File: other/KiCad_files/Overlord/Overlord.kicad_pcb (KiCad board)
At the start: 2 copper layers, 155.1 x 86.1 mm, 121 parts, among them J1 RJ45x2, J2 Screw_Terminal_01x09, J3 Screw_Terminal_01x09, J4 Screw_Terminal_01x09, J5 Screw_Terminal_01x09, J6 Screw_Terminal_01x09, J7 Conn_01x06_Male, Q1 2N7002E, Q2 2N7002E, Q3 2N7002E, Q4 2N7002E, Q5 2N7002E, Q6 2N7002E, U1 74HC4052D,653, U2 74HC4052D,653, U3 74HC4052D,653, U4 74HC4052D,653, U5 LM2575D2T-5G, U6 SN65HVD230, U7 MAX485ESA+T, U8 AP63203WU-7, U9 MAX485ESA+T

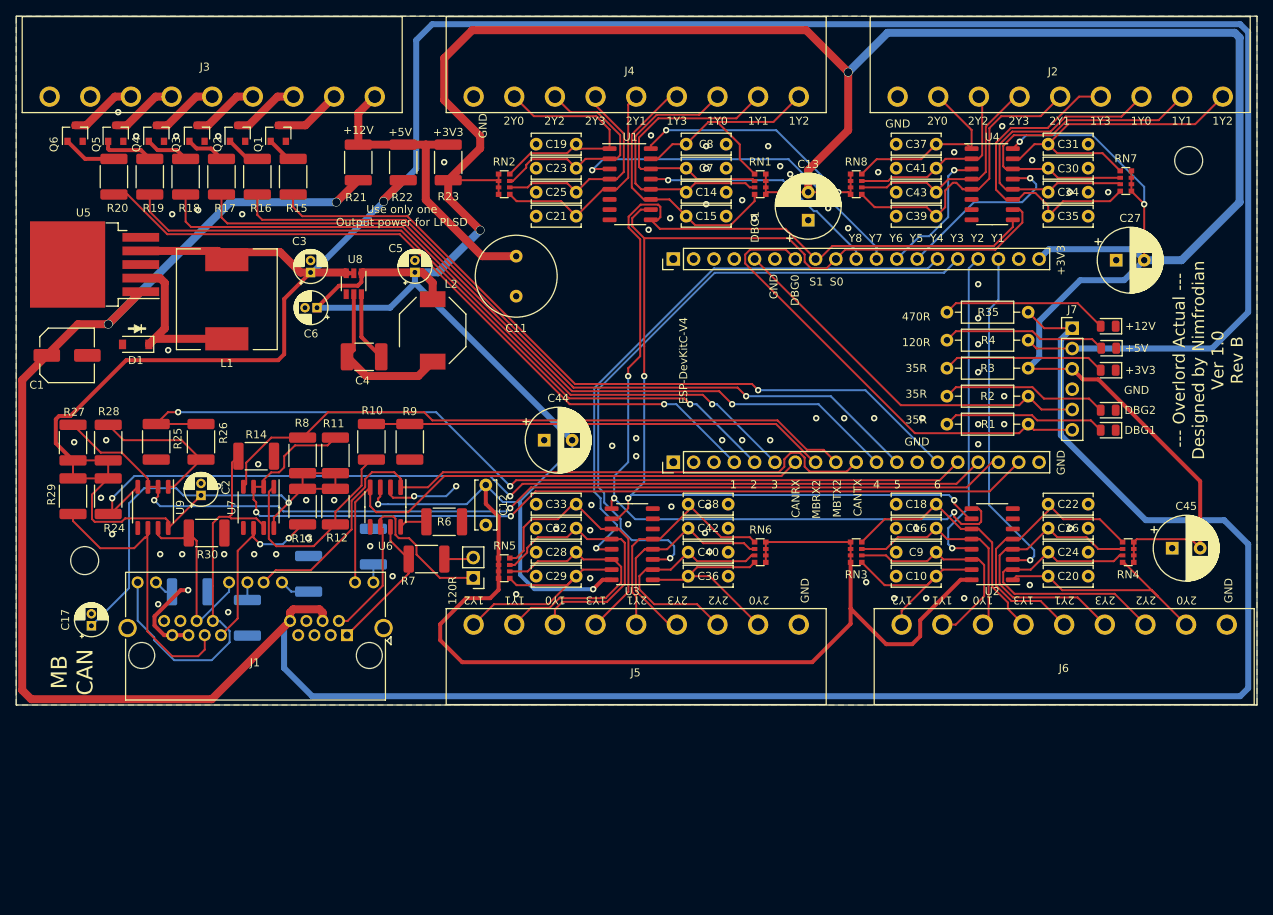
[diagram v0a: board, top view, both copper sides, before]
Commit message: Added LED pins for quick status display,  updated schematic (still need to update PCB),
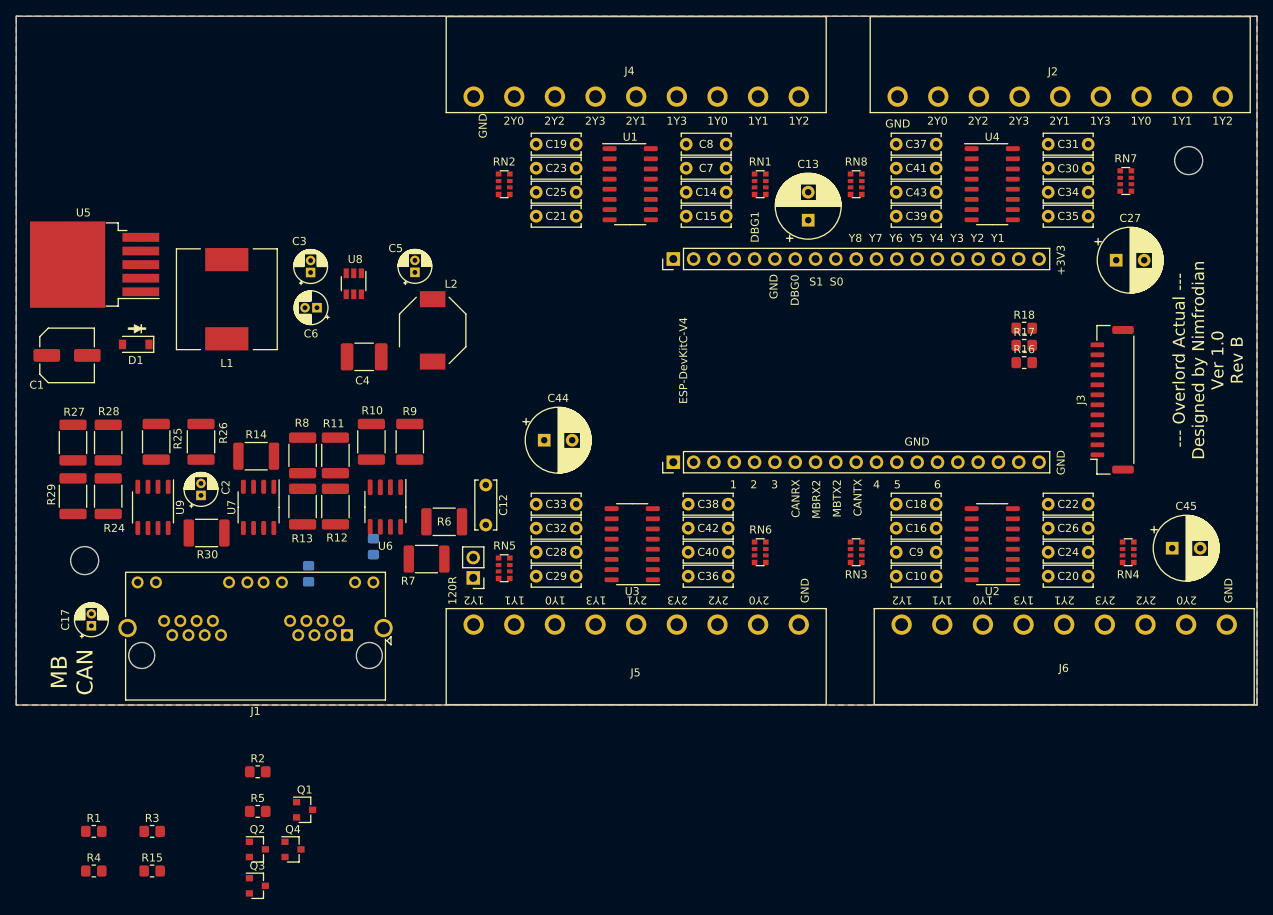
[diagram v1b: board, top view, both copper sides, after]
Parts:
- removed C11: 1800uF, Capacitor_THT:C_Radial_D10.0mm_H20.0mm_P5.00mm
- removed D2, D3, D4, D5, D6: LED, LED_SMD:LED_0805_2012Metric
- removed J7: Conn_01x06_Male, Connector_PinHeader_2.54mm:PinHeader_1x06_P2.54mm_Vertical
- removed Q5, Q6: 2N7002E, Package_TO_SOT_SMD:SOT-23
- removed R19, R20: 1K, Resistor_SMD:R_1812_4532Metric_Pad1.30x3.40mm_HandSolder
- removed R21: V_select_12V, Resistor_SMD:R_1812_4532Metric_Pad1.30x3.40mm_HandSolder
- removed R22: V_select_5V, Resistor_SMD:R_1812_4532Metric_Pad1.30x3.40mm_HandSolder
- removed R23: V_select_3V3, Resistor_SMD:R_1812_4532Metric_Pad1.30x3.40mm_HandSolder
- removed R32, R34: 220, Resistor_SMD:R_1812_4532Metric_Pad1.30x3.40mm_HandSolder
- removed R35: 470R, Resistor_THT:R_Axial_DIN0207_L6.3mm_D2.5mm_P10.16mm_Horizontal
- added R5: 10K, Resistor_SMD:R_0805_2012Metric_Pad1.20x1.40mm_HandSolder, F.Cu at (55.6, 124.8)
- J3: value Screw_Terminal_01x09 -> Conn_01x12_Female; footprint TerminalBlockCustom:TerminalBlock_9_5.08mm -> Connector_Molex:Molex_CLIK-Mate_502386-1270_1x12-1MP_P1.25mm_Horizontal
- R1, R2: value 35R -> 5K; footprint Resistor_THT:R_Axial_DIN0207_L6.3mm_D2.5mm_P10.16mm_Horizontal -> Resistor_SMD:R_0805_2012Metric_Pad1.20x1.40mm_HandSolder
- R15: value 1K -> 10K; footprint Resistor_SMD:R_1812_4532Metric_Pad1.30x3.40mm_HandSolder -> Resistor_SMD:R_0805_2012Metric_Pad1.20x1.40mm_HandSolder
- R16, R17, R18: value 1K -> 220; footprint Resistor_SMD:R_1812_4532Metric_Pad1.30x3.40mm_HandSolder -> Resistor_SMD:R_0805_2012Metric_Pad1.20x1.40mm_HandSolder
- R3: value 35R -> 10K; footprint Resistor_THT:R_Axial_DIN0207_L6.3mm_D2.5mm_P10.16mm_Horizontal -> Resistor_SMD:R_0805_2012Metric_Pad1.20x1.40mm_HandSolder
- R31, R33: value 220 -> 5K; footprint Resistor_SMD:R_1812_4532Metric_Pad1.30x3.40mm_HandSolder -> Resistor_SMD:R_0805_2012Metric_Pad1.20x1.40mm_HandSolder
- R4: value 120R -> 10K; footprint Resistor_THT:R_Axial_DIN0207_L6.3mm_D2.5mm_P10.16mm_Horizontal -> Resistor_SMD:R_0805_2012Metric_Pad1.20x1.40mm_HandSolder
- moved R4 134.3 mm to (35.1, 132.2), turned to 0 degrees
- moved R1 127.4 mm to (35.1, 127.3), turned to 0 degrees
- moved R3 123.9 mm to (42.4, 127.3), turned to 0 degrees
- moved J3 118.7 mm to (162.4, 73.3), turned to 90 degrees
- moved R2 107.1 mm to (55.6, 119.8), turned to 0 degrees
- moved R18 106.5 mm to (151.4, 64.4), turned to 0 degrees
- moved R17 102.5 mm to (151.4, 66.5), turned to 0 degrees
- moved R16 98.6 mm to (151.4, 68.7), turned to 0 degrees
- moved Q3 94.4 mm to (55.5, 134.1), turned to 0 degrees
- moved Q4 91.1 mm to (60.0, 129.6), turned to 0 degrees
- moved Q2 89.5 mm to (55.5, 129.6), turned to 0 degrees
- moved R15 88.6 mm to (42.4, 132.2), turned to 0 degrees
- moved Q1 84.6 mm to (61.5, 124.6), turned to 0 degrees
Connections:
- net MB_A_0+ renamed MB_A_1+
- net MB_DIR_CTRL_U0 renamed MB_DIR_CTRL_U1
- ESP1 pad 11: LP-LSD4 -> MB_TX_U1
- ESP1 pad 12: LP-LSD5 -> MB_RX_U1
- ESP1 pad 14: LP-LSD6 -> Net-(ESP1-Pad14)
- ESP1 pad 15: MB_RX_U0 -> UART_RX_0
- ESP1 pad 16: MB_TX_U0 -> UART_TX_0
- ESP1 pad 24: DEBUG_1 -> Net-(ESP1-Pad24)
- ESP1 pad 26: DEBUG_0 -> Net-(ESP1-Pad26)
- ESP1 pad 4: LP-LSD1 -> STATUS_LED_R
- ESP1 pad 5: LP-LSD2 -> STATUS_LED_G
- ESP1 pad 6: LP-LSD3 -> STATUS_LED_B
- J1 pad 10: CAN_RX -> Net-(J1-Pad10)
- J1 pad 12: CAN_TX -> Net-(J1-Pad12)
- J1 pad 16: MB_B_0- -> +5V
- J1 pad 18: Net-(J1-Pad18) -> MB_B_1-
- J1 pad 20: Net-(J1-Pad20) -> +3V3
- J1 pad 22: MB_B_0- -> Net-(J1-Pad22)
- J1 pad 24: MB_B_2- -> Net-(J1-Pad24)
- J3 pad 1: Net-(C11-Pad2) -> MB_RX_U2
- J3 pad 2: Net-(J3-Pad2) -> MB_TX_U2
- J3 pad 3: Net-(J3-Pad3) -> MB_TX_U1
- J3 pad 4: Net-(J3-Pad4) -> MB_RX_U1
- J3 pad 5: Net-(J3-Pad5) -> UART_RX_0
- J3 pad 6: Net-(J3-Pad6) -> UART_TX_0
- J3 pad 7: Net-(J3-Pad7) -> GND
- J3 pad 8: GND -> CAN_H
- J3 pad 9: GND -> CAN_L
- Q1 pad 3: Net-(J3-Pad2) -> Net-(J1-Pad9)
- Q2 pad 3: Net-(J3-Pad3) -> Net-(J1-Pad23)
- Q3 pad 3: Net-(J3-Pad4) -> Net-(J1-Pad11)
- Q4 pad 3: Net-(J3-Pad5) -> Net-(J1-Pad21)
- R1 pad 1: DEBUG_0 -> Net-(J1-Pad24)
- R1 pad 2: Net-(D2-Pad2) -> +12V
- R15 pad 1: LP-LSD6 -> Net-(Q4-Pad1)
- R15 pad 2: Net-(Q1-Pad1) -> MB_B_1-
- R16 pad 1: LP-LSD5 -> Net-(J3-Pad10)
- R16 pad 2: Net-(Q2-Pad1) -> STATUS_LED_R
- R17 pad 1: LP-LSD4 -> Net-(J3-Pad11)
- R17 pad 2: Net-(Q3-Pad1) -> STATUS_LED_G
- R18 pad 1: LP-LSD3 -> Net-(J3-Pad12)
- R18 pad 2: Net-(Q4-Pad1) -> STATUS_LED_B
- R2 pad 1: DEBUG_1 -> Net-(J1-Pad22)
- R2 pad 2: Net-(D3-Pad2) -> +12V
- R24 pad 2: MB_TX_U0 -> MB_TX_U1
- R25 pad 2: MB_RX_U0 -> MB_RX_U1
- R26 pad 1: MB_RX_U0 -> MB_RX_U1
- R3 pad 1: +3V3 -> Net-(Q1-Pad1)
- R3 pad 2: Net-(D4-Pad2) -> CAN_TX
- R30 pad 1: MB_B_0- -> MB_B_1-
- R31 pad 1: GND -> Net-(J1-Pad12)
- R31 pad 2: Net-(J1-Pad11) -> +12V
- R33 pad 1: Net-(J1-Pad9) -> Net-(J1-Pad10)
- R33 pad 2: GND -> +12V
- R4 pad 1: +5V -> Net-(Q2-Pad1)
- R4 pad 2: Net-(D5-Pad2) -> MB_B_2-
- U9 pad 4: MB_TX_U0 -> MB_TX_U1
- U9 pad 7: MB_B_0- -> MB_B_1-
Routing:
- net +3V3: track 606.1 -> 0.00 mm, vias 8 -> 0
- net +5V: track 379.6 -> 0.00 mm, vias 2 -> 0
- net +12V: track 337.4 -> 0.00 mm, vias 2 -> 0
- net S1: track 146.8 -> 0.00 mm, vias 3 -> 0
- net S0: track 142.1 -> 0.00 mm, vias 3 -> 0
- net MB_DIR_CTRL_U1: track 125.0 -> 0.00 mm, vias 2 -> 0
- net MB_TX_U0: track 119.5 -> 0.00 mm, vias 2 -> 0
- net MB_DIR_CTRL_U2: track 115.7 -> 0.00 mm, vias 2 -> 0
- net MB_RX_U0: track 111.5 -> 0.00 mm, vias 2 -> 0
- net LP-LSD4: track 97.4 -> 0.00 mm, vias 1 -> 0
- net LP-LSD6: track 95.3 -> 0.00 mm, vias 1 -> 0
- net LP-LSD5: track 95.3 -> 0.00 mm, vias 1 -> 0
- net LP-LSD1: track 91.4 -> 0.00 mm, vias 1 -> 0
- net LP-LSD2: track 90.7 -> 0.00 mm, vias 1 -> 0
- net LP-LSD3: track 89.5 -> 0.00 mm, vias 1 -> 0
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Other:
- board text removed: "+12V"
- board text removed: "+5V"
- board text removed: "470R 120R 35R 35R 35R"
- board text removed: "DBG2"
- board text removed: "Use only one Output power for LPLSD"

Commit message: Finalised ver1.0 revC of PCB Added interface PCB
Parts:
- added D2: D, Diode_SMD:D_SOD-123, F.Cu at (55.4, 46.9)
- added J7: USB_B, Connector_USB:USB_B_OST_USB-B1HSxx_Horizontal, F.Cu at (62.5, 41.2)
- added J8: USB_cable, Connector_PinHeader_2.54mm:PinHeader_1x04_P2.54mm_Vertical, F.Cu at (67.5, 46.4)
- ESP1: footprint roomcontroller:ESP32-DevKitC-V4 -> Overlord:ESP32-DevKitC-V4
- Q1, Q2, Q3, Q4, R1, R15, R2, R3, R4, R5: moved to B.Cu
- moved R3 47.5 mm to (74.7, 92.4), turned to -90 degrees
- moved Q3 44.5 mm to (64.9, 90.6), turned to -90 degrees
- moved R4 44.3 mm to (46.8, 89.5)
- moved Q2 41.1 mm to (42.9, 90.5), turned to -90 degrees
- moved Q4 39.9 mm to (51.7, 90.6), turned to -90 degrees
- moved R1 35.9 mm to (56.7, 98.6)
- moved R15 35.1 mm to (45.0, 97.2), turned to -90 degrees
- moved Q1 35.1 mm to (70.0, 90.6), turned to -90 degrees
- moved R5 32.4 mm to (64.9, 93.7)
- moved R2 24.0 mm to (47.3, 97.3), turned to -90 degrees
- moved C6 21.7 mm to (84.3, 57.7), turned to -90 degrees
- moved U5 20.8 mm to (41.3, 36.5), turned to 90 degrees
- moved C1 12.5 mm to (32.6, 55.3)
- moved R31 11.4 mm to (59.1, 106.1), turned to 0 degrees
- moved C5 10.4 mm to (82.1, 49.6)
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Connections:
- net +3V3 renamed +3.3V
- ESP1 pad 1: Net-(ESP1-Pad1) -> unconnected-(ESP1-CLK-Pad1)
- ESP1 pad 14: Net-(ESP1-Pad14) -> unconnected-(ESP1-D22-Pad14)
- ESP1 pad 2: Net-(ESP1-Pad2) -> unconnected-(ESP1-D0-Pad2)
- ESP1 pad 20: Net-(ESP1-Pad20) -> unconnected-(ESP1-+5V-Pad20)
- ESP1 pad 21: Net-(ESP1-Pad21) -> unconnected-(ESP1-CMD-Pad21)
- ESP1 pad 22: Net-(ESP1-Pad22) -> unconnected-(ESP1-D3-Pad22)
- ESP1 pad 23: Net-(ESP1-Pad23) -> unconnected-(ESP1-D2-Pad23)
- ESP1 pad 24: Net-(ESP1-Pad24) -> unconnected-(ESP1-D13-Pad24)
- ESP1 pad 26: Net-(ESP1-Pad26) -> unconnected-(ESP1-D12-Pad26)
- ESP1 pad 3: Net-(ESP1-Pad3) -> unconnected-(ESP1-D1-Pad3)
- ESP1 pad 37: Net-(ESP1-Pad37) -> unconnected-(ESP1-EN-Pad37)
- J1 pad 3: Net-(J1-Pad3) -> unconnected-(J1-Pad3)
- J1 pad 6: Net-(J1-Pad6) -> unconnected-(J1-Pad6)
- J3 pad MP: (no net) -> GND
- U1 pad 7: GND -> unconnected-(U1-VEE-Pad7)
- U2 pad 7: GND -> unconnected-(U2-VEE-Pad7)
- U3 pad 7: GND -> unconnected-(U3-VEE-Pad7)
- U4 pad 7: GND -> unconnected-(U4-VEE-Pad7)
- U6 pad 5: Net-(U6-Pad5) -> unconnected-(U6-Vref-Pad5)
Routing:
- net +3.3V: track 0.00 -> 605.9 mm, vias 0 -> 6
- net +5V: track 0.00 -> 274.6 mm, vias 0 -> 2
- net CAN_L: track 0.00 -> 193.3 mm, vias 0 -> 1
- net CAN_H: track 0.00 -> 173.6 mm
- net MB_TX_U1: track 0.00 -> 152.7 mm, vias 0 -> 3
- net S1: track 0.00 -> 148.8 mm, vias 0 -> 3
- net S0: track 0.00 -> 142.8 mm, vias 0 -> 3
- net +12V: track 0.00 -> 137.0 mm
- net MB_RX_U1: track 0.00 -> 136.9 mm, vias 0 -> 2
- net MB_DIR_CTRL_U1: track 0.00 -> 129.7 mm, vias 0 -> 2
- net MB_TX_U2: track 0.00 -> 117.4 mm, vias 0 -> 1
- net MB_DIR_CTRL_U2: track 0.00 -> 117.3 mm, vias 0 -> 2
- net MB_RX_U2: track 0.00 -> 95.9 mm, vias 0 -> 1
- net CAN_TX: track 0.00 -> 91.5 mm, vias 0 -> 1
- net Y3: track 0.00 -> 79.9 mm, vias 0 -> 1
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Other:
- net class Default removed
- board text added: "--- Overlord Actual --- Designed by Nimfrodian Ver 1.0 Rev C"
- board text added: "CAN"
- board text added: "MB"
- board text removed: "--- Overlord Actual --- Designed by Nimfrodian Ver 1.0 Rev B"
- board text removed: "MB CAN"
